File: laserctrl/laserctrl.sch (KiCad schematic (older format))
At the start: 17 parts, among them P1 JTAG, U1 LPC1769FBD100, X1 12MHz, X2 32768Hz

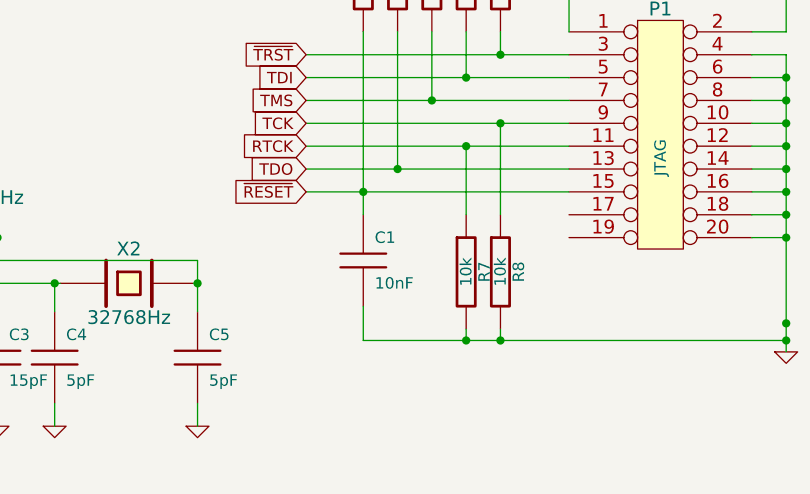
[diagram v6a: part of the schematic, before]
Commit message: Use double-shottky diodes in stead of tons of discrete miniMELFs
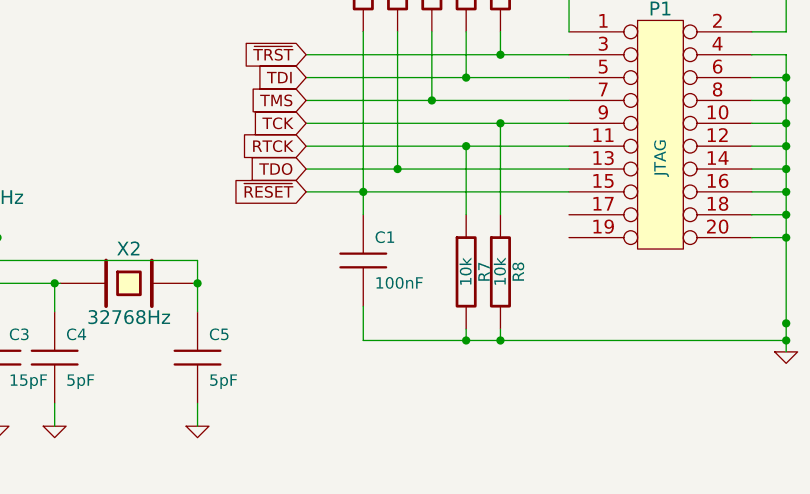
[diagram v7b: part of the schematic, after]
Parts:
- C1: value 10nF -> 100nF
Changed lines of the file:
@@
-EESchema Schematic File Version 2  date 2011-11-09T19:37:00 CET
+EESchema Schematic File Version 2  date 2011-11-09T22:36:32 CET
 LIBS:power
 LIBS:device
@@
 LIBS:microsd
 LIBS:jumper3
+LIBS:diode2
+LIBS:laserctrl-cache
 EELAYER 25  0
 EELAYER END
@@
 AD5
 $Comp
-L AGND #PWR8
+L AGND #PWR01
 U 1 1 4EB471B3
 P 2850 7450
-F 0 "#PWR8" H 2850 7450 40  0001 C CNN
+F 0 "#PWR01" H 2850 7450 40  0001 C CNN
 F 1 "AGND" H 2850 7380 50  0000 C CNN
 	1    2850 7450
@@
 $EndComp
 $Comp
-L GND #PWR7
+L GND #PWR02
 U 1 1 4EB47172
 P 2550 7450
-F 0 "#PWR7" H 2550 7450 30  0001 C CNN
+F 0 "#PWR02" H 2550 7450 30  0001 C CNN
 F 1 "GND" H 2550 7380 30  0001 C CNN
 	1    2550 7450
@@
 P 7050 6650
 F 0 "C1" H 7100 6750 50  0000 L CNN
-F 1 "10nF" H 7100 6550 50  0000 L CNN
+F 1 "100nF" H 7100 6550 50  0000 L CNN
 	1    7050 6650
 	1    0    0    -1
@@
 ~TRST
 $Comp
-L +3.3V #PWR1
+L +3.3V #PWR03
 U 1 1 4EA46529
 P 8900 5075
-F 0 "#PWR1" H 8900 5035 30  0001 C CNN
+F 0 "#PWR03" H 8900 5035 30  0001 C CNN
 F 1 "+3.3V" H 8900 5185 30  0000 C CNN
 	1    8900 5075
@@
 $EndComp
 $Comp
-L GND #PWR2
+L GND #PWR04
 U 1 1 4EA464E3
 P 8900 7050
-F 0 "#PWR2" H 8900 7050 30  0001 C CNN
+F 0 "#PWR04" H 8900 7050 30  0001 C CNN
 F 1 "GND" H 8900 6980 30  0001 C CNN
 	1    8900 7050
@@
 TDO
 $Comp
-L GND #PWR6
+L GND #PWR05
 U 1 1 4EA3EE94
 P 6325 7375
-F 0 "#PWR6" H 6325 7375 30  0001 C CNN
+F 0 "#PWR05" H 6325 7375 30  0001 C CNN
 F 1 "GND" H 6325 7305 30  0001 C CNN
 	1    6325 7375
@@
 $EndComp
 $Comp
-L GND #PWR5
+L GND #PWR06
 U 1 1 4EA3EE90
 P 5700 7375
-F 0 "#PWR5" H 5700 7375 30  0001 C CNN
+F 0 "#PWR06" H 5700 7375 30  0001 C CNN
 F 1 "GND" H 5700 7305 30  0001 C CNN
 	1    5700 7375
@@
 $EndComp
 $Comp
-L GND #PWR4
+L GND #PWR07
 U 1 1 4EA3EE8C
 P 5450 7375
-F 0 "#PWR4" H 5450 7375 30  0001 C CNN
+F 0 "#PWR07" H 5450 7375 30  0001 C CNN
 F 1 "GND" H 5450 7305 30  0001 C CNN
 	1    5450 7375
@@
 $EndComp
 $Comp
-L GND #PWR3
+L GND #PWR08
 U 1 1 4EA3EE86
 P 4775 7375
-F 0 "#PWR3" H 4775 7375 30  0001 C CNN
+F 0 "#PWR08" H 4775 7375 30  0001 C CNN
 F 1 "GND" H 4775 7305 30  0001 C CNN
 	1    4775 7375
@@
 $EndComp
 $Comp
-L +BATT #PWR11
+L +BATT #PWR09
 U 1 1 4EA3ED82
 P 4100 7450
-F 0 "#PWR11" H 4100 7400 20  0001 C CNN
+F 0 "#PWR09" H 4100 7400 20  0001 C CNN
 F 1 "+BATT" H 4100 7550 30  0000 C CNN
 	1    4100 7450
@@
 $EndComp
 $Comp
-L +3.3VADC #PWR10
+L +3.3VADC #PWR010
 U 1 1 4EA3EA65
 P 3800 7450
-F 0 "#PWR10" H 3800 7570 20  0001 C CNN
+F 0 "#PWR010" H 3800 7570 20  0001 C CNN
 F 1 "+3.3VADC" H 3800 7540 30  0000 C CNN
 	1    3800 7450
@@
 $EndComp
 $Comp
-L +3.3V #PWR9
+L +3.3V #PWR011
 U 1 1 4EA3EA51
 P 3400 7450
-F 0 "#PWR9" H 3400 7410 30  0001 C CNN
+F 0 "#PWR011" H 3400 7410 30  0001 C CNN
 F 1 "+3.3V" H 3400 7560 30  0000 C CNN
 	1    3400 7450
